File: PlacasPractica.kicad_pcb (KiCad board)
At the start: 2 copper layers, 71 parts, among them J1 USB_OTG, J2 Conn_01x10, J3 Conn_01x10, J4 CONN_02X05, SW1 SW_Push, U1 SAMD20J18A-AU, U2 XBEE, U3 MB85RC64VPNF-G-JNERE1, U4 XC6220B331MR-G, U5 XC6220B331MR-G, U6 XC6220B331MR-G, Y1 Crystal

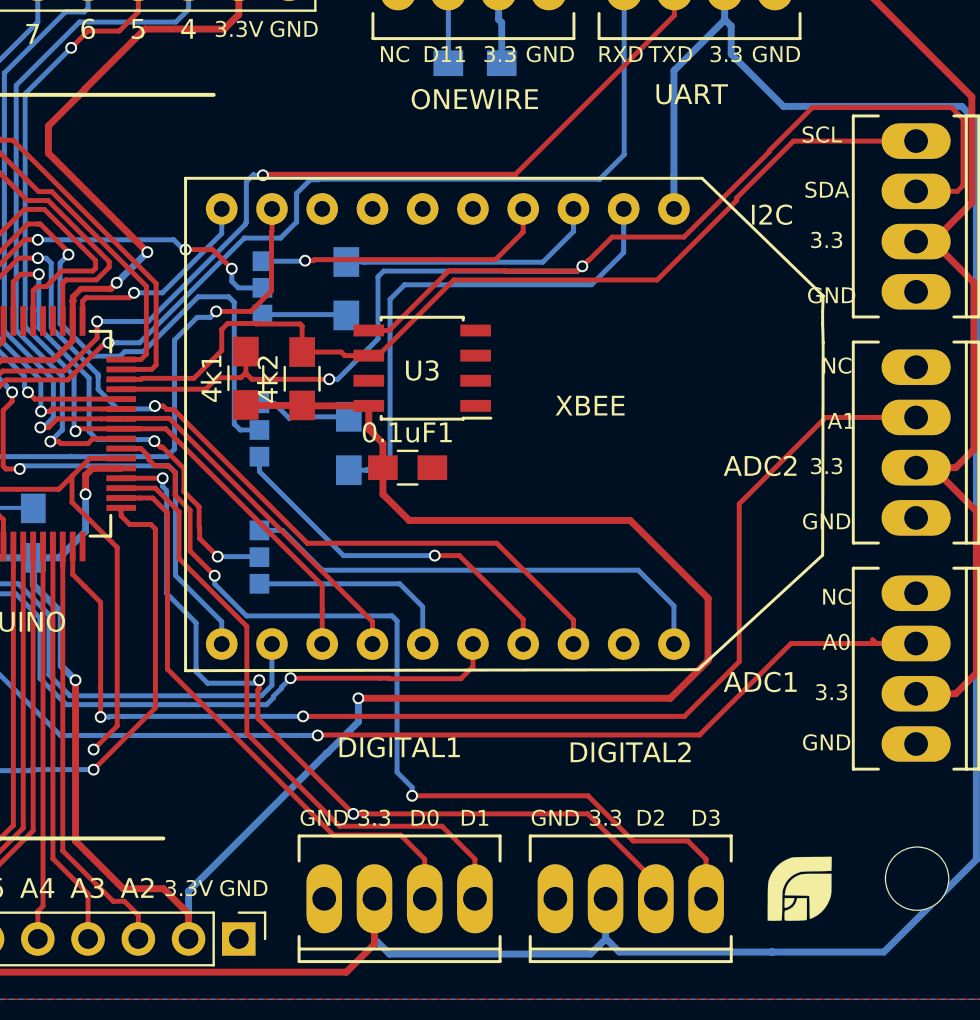
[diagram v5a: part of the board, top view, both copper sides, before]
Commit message: Placa final corregida.
Corregidas algunas pistas y definido correctamente la separación del plano de pasa respecto a las pistas de alimentación y de datos
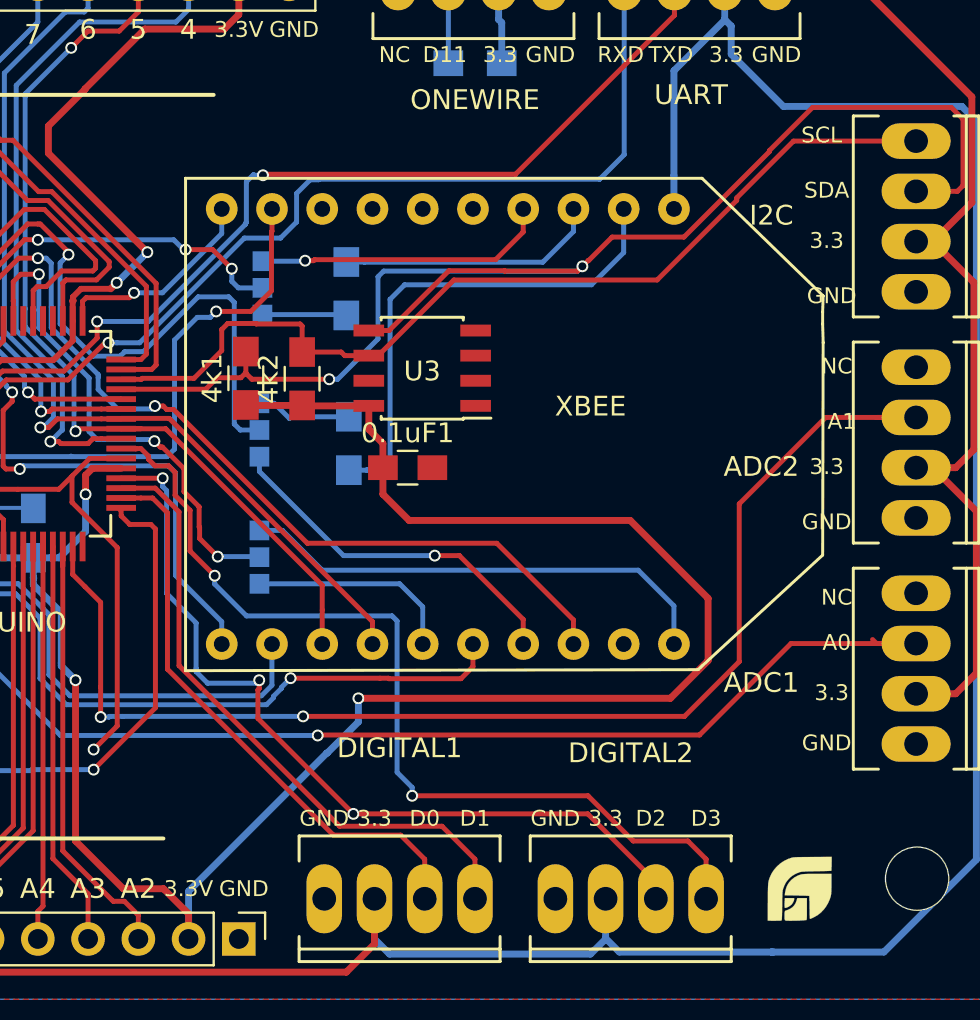
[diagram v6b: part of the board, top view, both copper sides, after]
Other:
- net class Alimentacion: clearance 0.2 -> 0.508
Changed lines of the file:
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@@
     (links 180)
     (no_connects 2)
-    (area 77.818857 56.325691 202.985507 134.454)
+    (area 77.510857 71.987 177.505143 134.762)
     (thickness 1.6)
-    (drawings 73)
-    (tracks 1133)
+    (drawings 69)
+    (tracks 1131)
     (zones 0)
     (modules 71)
@@
     (mod_text_size 1 1)
     (mod_text_width 0.15)
-    (pad_size 1.524 1.524)
-    (pad_drill 0.762)
+    (pad_size 1.80086 3.50012)
+    (pad_drill 1.19888)
     (pad_to_mask_clearance 0.2)
     (aux_axis_origin 0 0)
@@
     (uvia_dia 0.3)
     (uvia_drill 0.1)
-    (add_net /3V3)
-    (add_net /3V3_COM)
-    (add_net /3V3_SENS)
     (add_net /A0)
     (add_net /A1)
@@
   )
   (net_class Alimentacion ""
-    (clearance 0.2)
+    (clearance 0.508)
     (trace_width 0.45)
     (via_dia 0.6)
@@
     (uvia_drill 0.1)
     (add_net +5V)
+    (add_net /3V3)
+    (add_net /3V3_COM)
+    (add_net /3V3_SENS)
   )
   (module XBEE:XBEE (layer F.Cu)
@@
     (effects (font (size 0.5 0.5) (thickness 0.125)) (justify mirror))
   )
-  (gr_text ASSOC (at 136.398 109.982 360) (layer B.SilkS)
+  (gr_text ASSOC (at 136.398 109.982) (layer B.SilkS)
     (effects (font (size 0.5 0.5) (thickness 0.125)) (justify mirror))
   )
@@
     (effects (font (size 0.8 0.8) (thickness 0.2)))
   )
-  (gr_text A0 (at 163.576 112.522 360) (layer F.SilkS)
+  (gr_text A0 (at 163.576 112.522) (layer F.SilkS)
     (effects (font (size 0.8 0.8) (thickness 0.2)))
   )
-  (gr_text "3.3\n" (at 163.322 115.062 360) (layer F.SilkS)
+  (gr_text "3.3\n" (at 163.322 115.062) (layer F.SilkS)
     (effects (font (size 0.8 0.8) (thickness 0.2)))
   )
-  (gr_text GND (at 163.068 117.602 360) (layer F.SilkS)
+  (gr_text GND (at 163.068 117.602) (layer F.SilkS)
     (effects (font (size 0.8 0.8) (thickness 0.2)))
   )
-  (gr_text "A1\n" (at 163.83 101.346 360) (layer F.SilkS)
+  (gr_text "A1\n" (at 163.83 101.346) (layer F.SilkS)
     (effects (font (size 0.8 0.8) (thickness 0.2)))
   )
-  (gr_text 3.3 (at 163.068 103.632 360) (layer F.SilkS)
+  (gr_text 3.3 (at 163.068 103.632) (layer F.SilkS)
     (effects (font (size 0.8 0.8) (thickness 0.2)))
   )
-  (gr_text GND (at 163.068 106.426 360) (layer F.SilkS)
+  (gr_text GND (at 163.068 106.426) (layer F.SilkS)
     (effects (font (size 0.8 0.8) (thickness 0.2)))
   )
-  (gr_text "SCL\n" (at 162.814 86.868 360) (layer F.SilkS)
+  (gr_text "SCL\n" (at 162.814 86.868) (layer F.SilkS)
     (effects (font (size 0.8 0.8) (thickness 0.2)))
   )
-  (gr_text SDA (at 163.068 89.662 360) (layer F.SilkS)
+  (gr_text SDA (at 163.068 89.662) (layer F.SilkS)
     (effects (font (size 0.8 0.8) (thickness 0.2)))
   )
-  (gr_text 3.3 (at 163.068 92.202 360) (layer F.SilkS)
+  (gr_text 3.3 (at 163.068 92.202) (layer F.SilkS)
     (effects (font (size 0.8 0.8) (thickness 0.2)))
   )
-  (gr_text GND (at 163.322 94.996 360) (layer F.SilkS)
+  (gr_text GND (at 163.322 94.996) (layer F.SilkS)
     (effects (font (size 0.8 0.8) (thickness 0.2)))
   )
@@
   )
   (gr_circle (center 113.284 90.424) (end 113.538 90.424) (layer F.SilkS) (width 0.2))
-  (dimension 88.9 (width 0.3) (layer Cmts.User)
-    (gr_text 88,900mm (at 128.27 57.675691) (layer Cmts.User)
-      (effects (font (size 1.5 1.5) (thickness 0.3)))
-    )
-    (feature1 (pts (xy 172.72 63.5) (xy 172.72 56.325691)))
-    (feature2 (pts (xy 83.82 63.5) (xy 83.82 56.325691)))
-    (crossbar (pts (xy 83.82 59.025691) (xy 172.72 59.025691)))
-    (arrow1a (pts (xy 172.72 59.025691) (xy 171.593496 59.612112)))
-    (arrow1b (pts (xy 172.72 59.025691) (xy 171.593496 58.43927)))
-    (arrow2a (pts (xy 83.82 59.025691) (xy 84.946504 59.612112)))
-    (arrow2b (pts (xy 83.82 59.025691) (xy 84.946504 58.43927)))
-  )
-  (dimension 2.54 (width 0.3) (layer Cmts.User)
-    (gr_text 2,540mm (at 130.81 67.23) (layer Cmts.User)
-      (effects (font (size 1.5 1.5) (thickness 0.3)))
-    )
-    (feature1 (pts (xy 132.08 127.508) (xy 132.08 65.88)))
-    (feature2 (pts (xy 129.54 127.508) (xy 129.54 65.88)))
-    (crossbar (pts (xy 129.54 68.58) (xy 132.08 68.58)))
-    (arrow1a (pts (xy 132.08 68.58) (xy 130.953496 69.166421)))
-    (arrow1b (pts (xy 132.08 68.58) (xy 130.953496 67.993579)))
-    (arrow2a (pts (xy 129.54 68.58) (xy 130.666504 69.166421)))
-    (arrow2b (pts (xy 129.54 68.58) (xy 130.666504 67.993579)))
-  )
-  (dimension 50.800635 (width 0.3) (layer Cmts.User)
-    (gr_text 50,801mm (at 187.165138 103.126069 270.2864765) (layer Cmts.User)
-      (effects (font (size 1.5 1.5) (thickness 0.3)))
-    )
-    (feature1 (pts (xy 136.906 128.778) (xy 188.642121 128.519319)))
-    (feature2 (pts (xy 136.652 77.978) (xy 188.388121 77.719319)))
-    (crossbar (pts (xy 185.688155 77.732819) (xy 185.942155 128.532819)))
-    (arrow1a (pts (xy 185.942155 128.532819) (xy 185.350109 127.409261)))
-    (arrow1b (pts (xy 185.942155 128.532819) (xy 186.522936 127.403397)))
-    (arrow2a (pts (xy 185.688155 77.732819) (xy 185.107374 78.862241)))
-    (arrow2b (pts (xy 185.688155 77.732819) (xy 186.280201 78.856377)))
-  )
-  (dimension 56.64257 (width 0.3) (layer Cmts.User)
-    (gr_text 56,643mm (at 197.056935 101.952166 270.25693) (layer Cmts.User)
-      (effects (font (size 1.5 1.5) (thickness 0.3)))
-    )
-    (feature1 (pts (xy 190.754 130.302) (xy 198.533922 130.267112)))
-    (feature2 (pts (xy 190.5 73.66) (xy 198.279922 73.625112)))
-    (crossbar (pts (xy 195.579949 73.63722) (xy 195.833949 130.27922)))
-    (arrow1a (pts (xy 195.833949 130.27922) (xy 195.242483 129.155357)))
-    (arrow1b (pts (xy 195.833949 130.27922) (xy 196.415312 129.150098)))
-    (arrow2a (pts (xy 195.579949 73.63722) (xy 194.998586 74.766342)))
-    (arrow2b (pts (xy 195.579949 73.63722) (xy 196.171415 74.761083)))
-  )
   (gr_text RESET (at 106.68 86.106) (layer F.SilkS)
     (effects (font (size 1 1) (thickness 0.25)))
@@
   (segment (start 87.1982 97.3262) (end 88.2982 97.3262) (width 0.25) (layer F.Cu) (net 23))
   (segment (start 88.2982 97.3262) (end 88.3048 97.3328) (width 0.25) (layer F.Cu) (net 23))
-  (segment (start 145.288 125.476) (end 145.288 123.47594) (width 0.25) (layer F.Cu) (net 24))
-  (segment (start 145.288 123.47594) (end 143.620461 121.808401) (width 0.25) (layer F.Cu) (net 24))
-  (segment (start 130.3274 105.91659) (end 129.12681 104.716) (width 0.25) (layer F.Cu) (net 24))
-  (segment (start 143.620461 121.808401) (end 138.445401 121.808401) (width 0.25) (layer F.Cu) (net 24))
-  (segment (start 138.445401 121.808401) (end 133.7564 117.1194) (width 0.25) (layer F.Cu) (net 24))
-  (segment (start 133.7564 111.7092) (end 130.3274 108.2802) (width 0.25) (layer F.Cu) (net 24))
-  (segment (start 133.7564 117.1194) (end 133.7564 111.7092) (width 0.25) (layer F.Cu) (net 24))
-  (segment (start 130.3274 108.2802) (end 130.3274 105.91659) (width 0.25) (layer F.Cu) (net 24))
-  (segment (start 129.12681 104.716) (end 127.402 104.716) (width 0.25) (layer F.Cu) (net 24))
+  (segment (start 127.402 104.716) (end 129.12681 104.716) (width 0.25) (layer F.Cu) (net 24))
+  (segment (start 129.12681 104.716) (end 130.3274 105.91659) (width 0.25) (layer F.Cu) (net 24))
+  (segment (start 130.3274 105.91659) (end 130.3274 113.6904) (width 0.25) (layer F.Cu) (net 24))
+  (segment (start 145.288 123.47594) (end 145.288 125.476) (width 0.25) (layer F.Cu) (net 24))
+  (segment (start 130.3274 113.6904) (end 138.445401 121.808401) (width 0.25) (layer F.Cu) (net 24))
+  (segment (start 138.445401 121.808401) (end 143.620461 121.808401) (width 0.25) (layer F.Cu) (net 24))
+  (segment (start 143.620461 121.808401) (end 145.288 123.47594) (width 0.25) (layer F.Cu) (net 24))
   (segment (start 142.748 125.476) (end 142.748 123.47594) (width 0.25) (layer F.Cu) (net 25))
   (segment (start 138.133411 122.258411) (end 129.7432 113.8682) (width 0.25) (layer F.Cu) (net 25))
@@
   (segment (start 124.8918 103.124) (end 124.8664 103.0986) (width 0.25) (layer B.Cu) (net 85))
   (zone (net 1) (net_name GND) (layer B.Cu) (hatch edge 0.508)
-    (connect_pads (clearance 0.25))
+    (connect_pads (clearance 0.2508))
     (min_thickness 0.254)
     (fill yes (arc_segments 16) (thermal_gap 0.508) (thermal_bridge_width 0.508) (smoothing fillet) (radius 2))

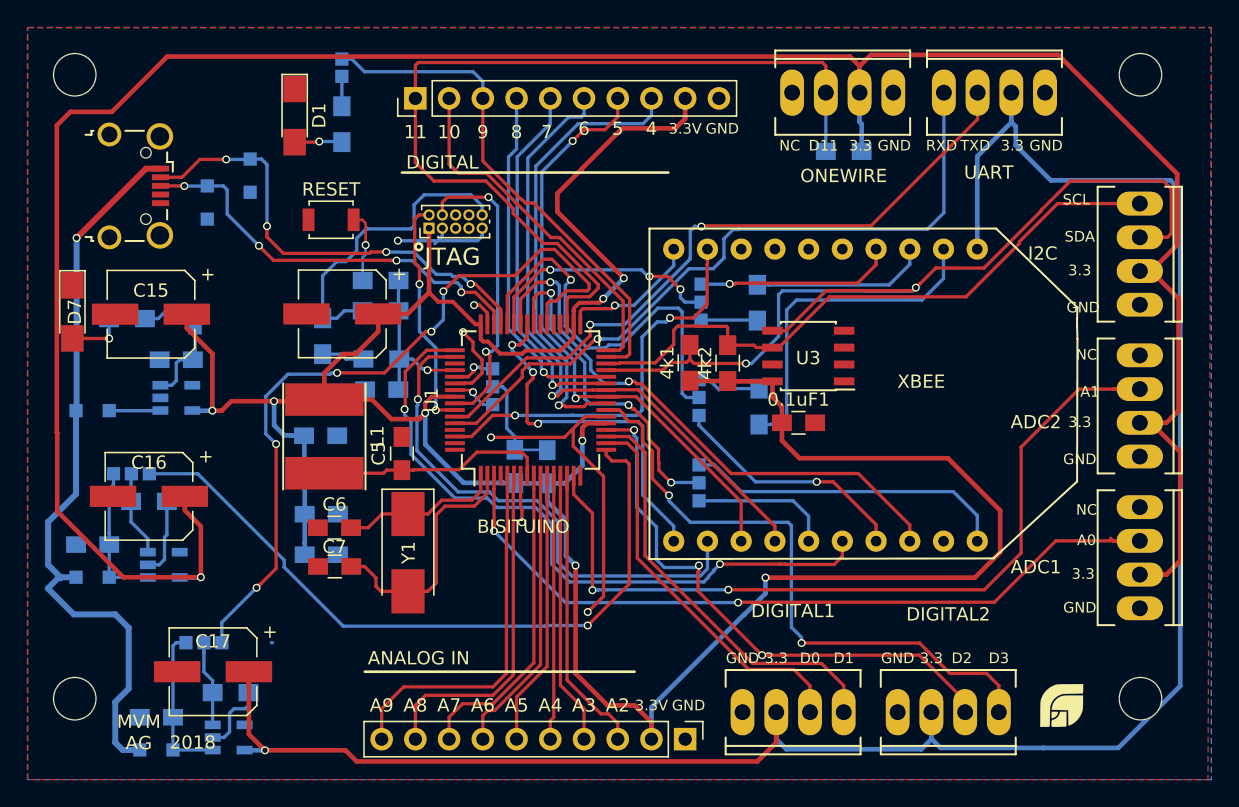
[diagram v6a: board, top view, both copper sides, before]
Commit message: Serigrafia corregida
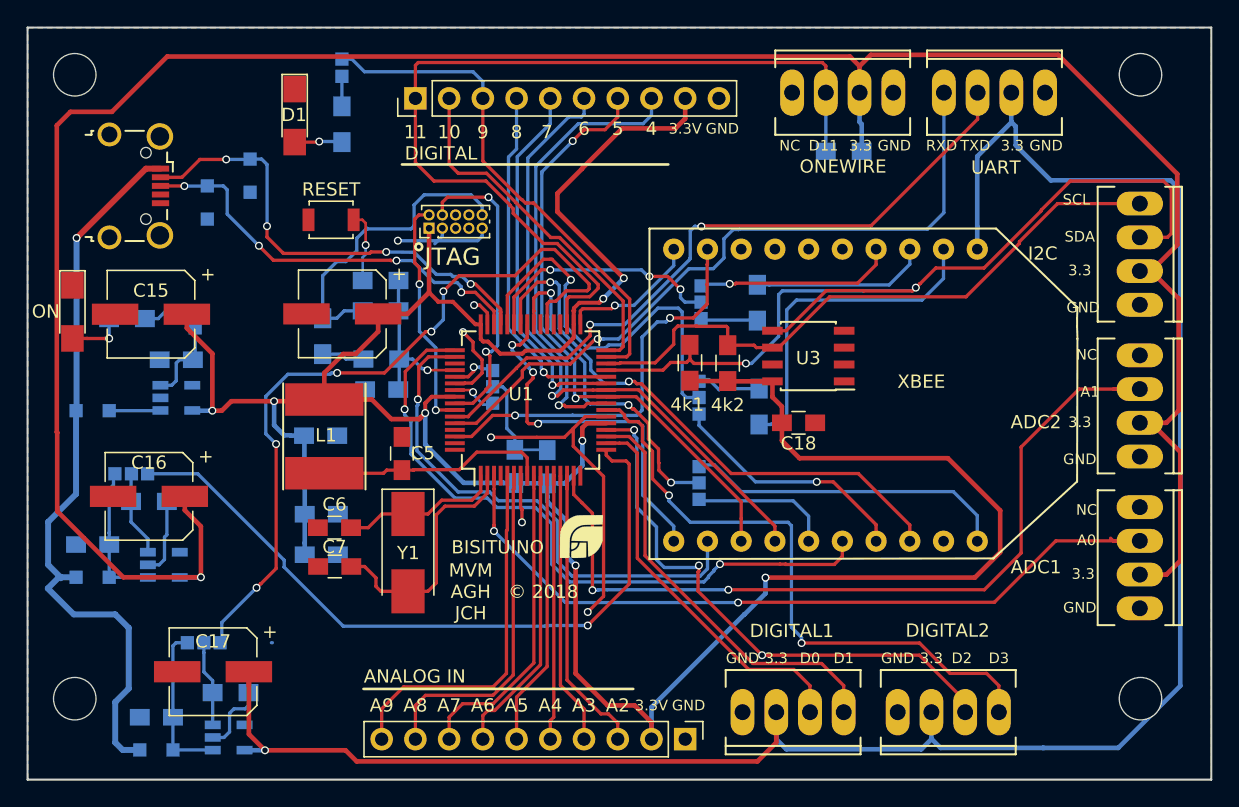
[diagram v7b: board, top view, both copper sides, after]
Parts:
- C11: value CP -> 100nF
- C12, C13: value C -> 4.7uF
- C14: value C -> 4,7uF
- C15, C16, C17: value CP -> 47uF
- C6, C7: value C -> 6.8pF
- D2, D3: value D_Zener_Small -> 5V1
- R1, R3, R4: value R_Small -> 330
- R5, R9: value R -> 330
- R6: value R -> 10k
- Y1: value Crystal -> 48MHz
- moved G*** 38.3 mm to (125.6, 110.7)
- renumbered 0.1uF1 to C18, D7 to ON
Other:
- board outline added: 89.2 x 56.6 mm
- board text added: "MVM AGH JCH"
- board text added: "© 2018"
- board text removed: "2018"
- board text removed: "MVM AG"

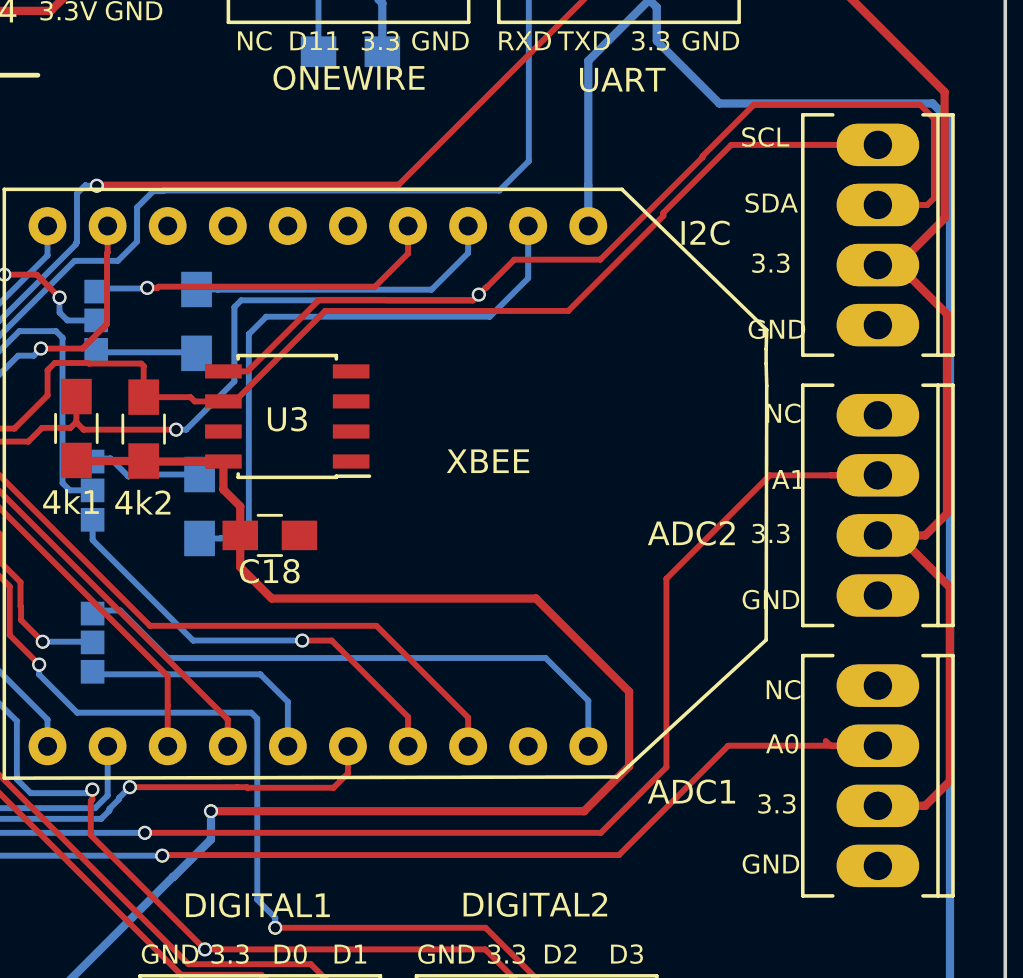
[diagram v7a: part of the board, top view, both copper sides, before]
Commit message: Chip criptografico en pcb añadido.
Se han añadido los chips para el encriptado en el esquematico y el diseño en pcb y actualizado la lista de materiales.
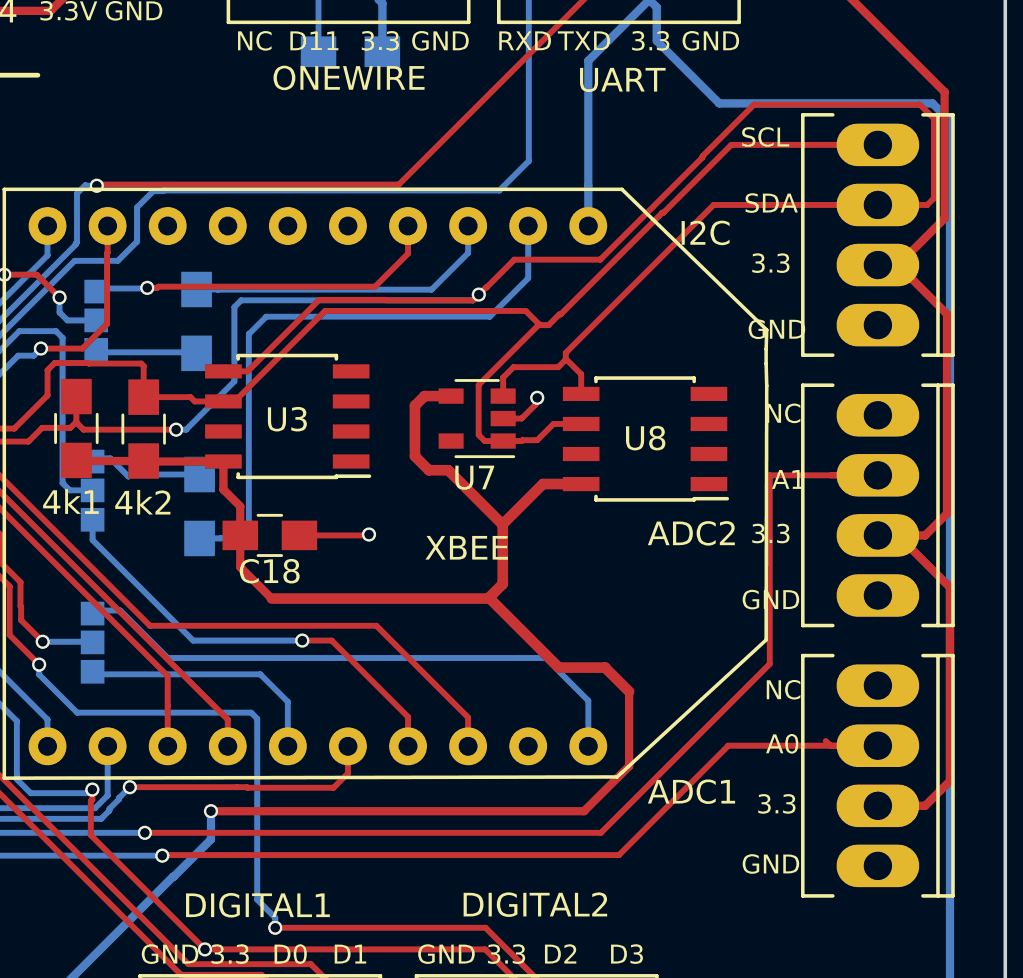
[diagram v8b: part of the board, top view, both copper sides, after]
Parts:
- added U7: 24AA02, TO_SOT_Packages_SMD:SOT-23-5, F.Cu at (150.6, 98.7)
- added U8: ATSHA204A, Housings_SOIC:SOIC-8_3.9x4.9mm_Pitch1.27mm, F.Cu at (157.7, 99.6)
- C18: value C -> 0.1uF
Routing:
- net /SDA: track 69.9 -> 91.5 mm
- net /3V3: track 219.1 -> 235.2 mm
- net /SCL: track 48.0 -> 58.9 mm
- net GND: track 66.9 -> 72.3 mm, vias 7 -> 9
